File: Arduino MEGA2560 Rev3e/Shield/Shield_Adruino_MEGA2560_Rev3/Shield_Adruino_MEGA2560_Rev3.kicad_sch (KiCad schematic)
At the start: 16 parts

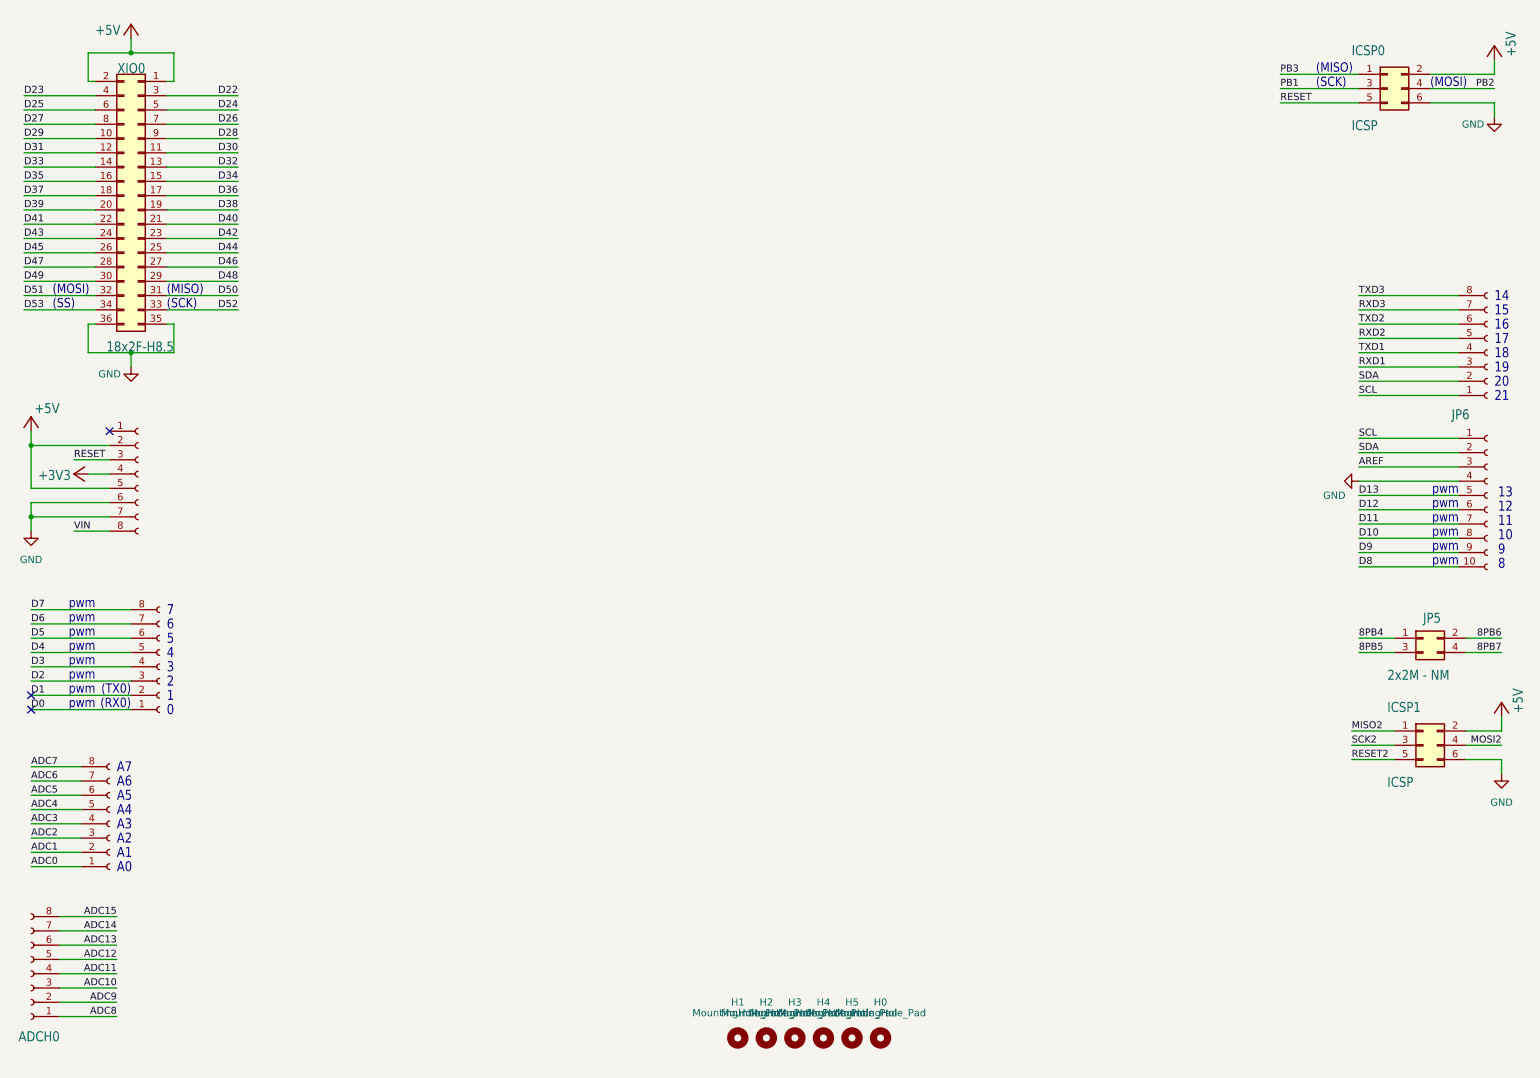
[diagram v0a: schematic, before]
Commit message: Update Shield_Adruino_MEGA2560_Rev3.kicad_pcb, Shield_Adruino_MEGA2560_Rev3.kicad_pro, and Shield_Adruino_MEGA2560_Rev3.kicad_sch to KiCad 7
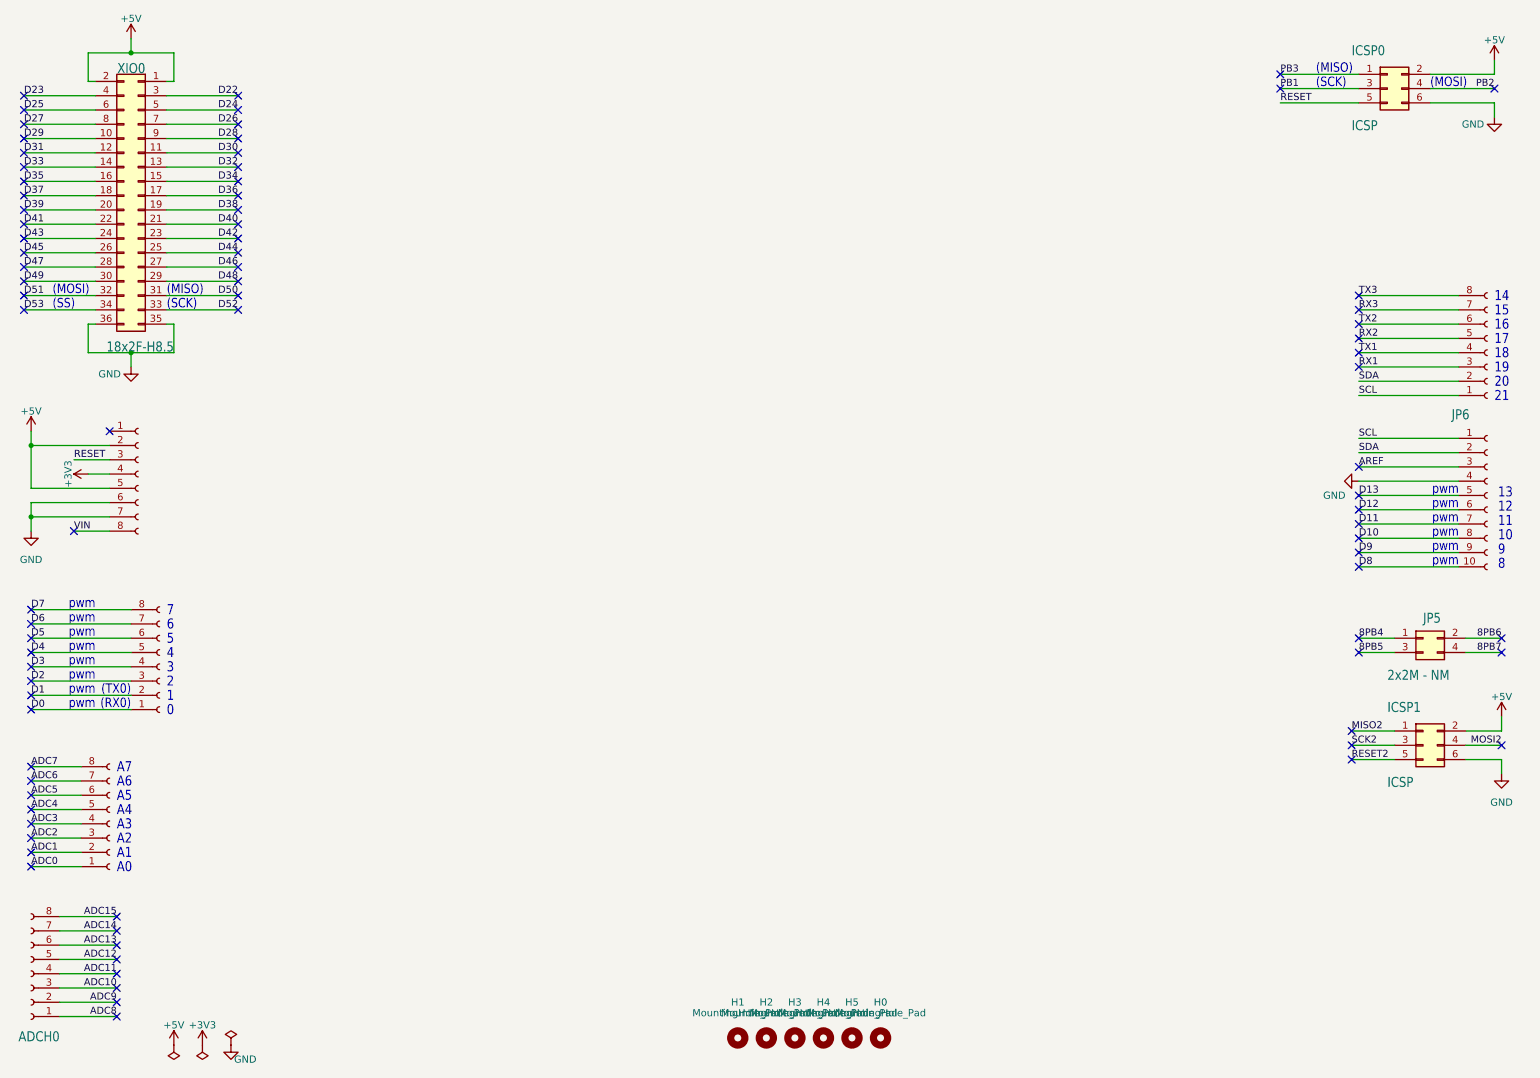
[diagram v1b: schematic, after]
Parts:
- ADCH0, ADCL0, COMMUNICATION0, POWER0, PWML0: symbol Connector:Conn_01x08_Female -> Connector:Conn_01x08_Socket
- JP6: symbol Connector:Conn_01x10_Female -> Connector:Conn_01x10_Socket
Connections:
- net RXD1 renamed RX1
- net RXD2 renamed RX2
- net RXD3 renamed RX3
- net TXD1 renamed TX1
- net TXD2 renamed TX2
- net TXD3 renamed TX3
- no-connect marks 3 -> 82
